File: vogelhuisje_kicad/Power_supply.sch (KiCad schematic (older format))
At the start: 8 parts, among them J1 Conn_01x02, J2 Conn_01x02_Female, J3 USB_C_Receptacle_USB2.0, P1 TP4056breakout, P2 GenericBoostConverter, Q1 Q_PMOS_GSD

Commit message: Update ESP_arduino.sch, Power_supply.sch, and 5 more files...
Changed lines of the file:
@@
 U 1 1 6263DE48
 P 2550 2300
-F 0 "P1" H 2575 2825 50  0000 C CNN
+F 0 "P?" H 2575 2825 50  0000 C CNN
 F 1 "TP4056breakout" H 2575 2734 50  0000 C CNN
 F 2 "Components:TP4056breakout" H 2500 2700 50  0001 C CNN
@@
 U 1 1 6263E192
 P 5450 2300
-F 0 "P2" H 5450 2715 50  0000 C CNN
+F 0 "P?" H 5450 2715 50  0000 C CNN
 F 1 "GenericBoostConverter" H 5450 2624 50  0000 C CNN
 F 2 "Components:GenericBoostConverter" H 5450 2450 50  0001 C CNN
@@
 U 1 1 6263EAD6
 P 3600 2250
-F 0 "R1" H 3670 2296 50  0000 L CNN
+F 0 "R?" H 3670 2296 50  0000 L CNN
 F 1 "100k" H 3670 2205 50  0000 L CNN
 F 2 "Resistor_THT:R_Axial_DIN0207_L6.3mm_D2.5mm_P7.62mm_Horizontal" V 3530 2250 50  0001 C CNN
@@
 U 1 1 6263EF5E
 P 1950 2400
-F 0 "#PWR0101" H 1950 2150 50  0001 C CNN
+F 0 "#PWR?" H 1950 2150 50  0001 C CNN
 F 1 "GND" H 1955 2227 50  0000 C CNN
 F 2 "" H 1950 2400 50  0001 C CNN
@@
 U 1 1 62643FC2
 P 3850 1900
-F 0 "D1" V 3896 1821 50  0000 R CNN
+F 0 "D?" V 3896 1821 50  0000 R CNN
 F 1 "D_Zener" V 3805 1821 50  0000 R CNN
 F 2 "Diode_SMD:D_SMB_Handsoldering" H 3850 1900 50  0001 C CNN
@@
 U 1 1 62647C4D
 P 3250 1200
-F 0 "J1" H 3168 875 50  0000 C CNN
+F 0 "J?" H 3168 875 50  0000 C CNN
 F 1 "Conn_01x02" H 3168 966 50  0000 C CNN
 F 2 "Connector_JST:JST_PH_B2B-PH-K_1x02_P2.00mm_Vertical" H 3250 1200 50  0001 C CNN
@@
 U 1 1 6264EDFF
 P 4100 1750
-F 0 "Q1" H 4305 1796 50  0000 L CNN
+F 0 "Q?" H 4305 1796 50  0000 L CNN
 F 1 "Q_PMOS_GSD" H 4305 1705 50  0000 L CNN
 F 2 "Package_TO_SOT_SMD:SOT-23" H 4300 1850 50  0001 C CNN
@@
 U 1 1 62654366
 P 5100 3300
-F 0 "J3" V 5253 4029 50  0000 L CNN
+F 0 "J?" V 5253 4029 50  0000 L CNN
 F 1 "USB_C_Receptacle_USB2.0" V 5162 4029 50  0000 L CNN
 F 2 "Connector_USB:USB_C_Receptacle_HRO_TYPE-C-31-M-12" H 5250 3300 50  0001 C CNN
@@
 U 1 1 62641E6A
 P 1650 2250
-F 0 "J2" H 1542 1925 50  0000 C CNN
+F 0 "J?" H 1542 1925 50  0000 C CNN
 F 1 "Conn_01x02_Female" H 1542 2016 50  0000 C CNN
 F 2 "Connector_PinSocket_2.54mm:PinSocket_1x02_P2.54mm_Vertical" H 1650 2250 50  0001 C CNN
@@
 U 1 1 62647069
 P 3600 2450
-F 0 "#PWR0102" H 3600 2200 50  0001 C CNN
+F 0 "#PWR?" H 3600 2200 50  0001 C CNN
 F 1 "GND" H 3605 2277 50  0000 C CNN
 F 2 "" H 3600 2450 50  0001 C CNN
@@
 U 1 1 626475C4
 P 6200 2450
-F 0 "#PWR0103" H 6200 2200 50  0001 C CNN
+F 0 "#PWR?" H 6200 2200 50  0001 C CNN
 F 1 "GND" H 6205 2277 50  0000 C CNN
 F 2 "" H 6200 2450 50  0001 C CNN

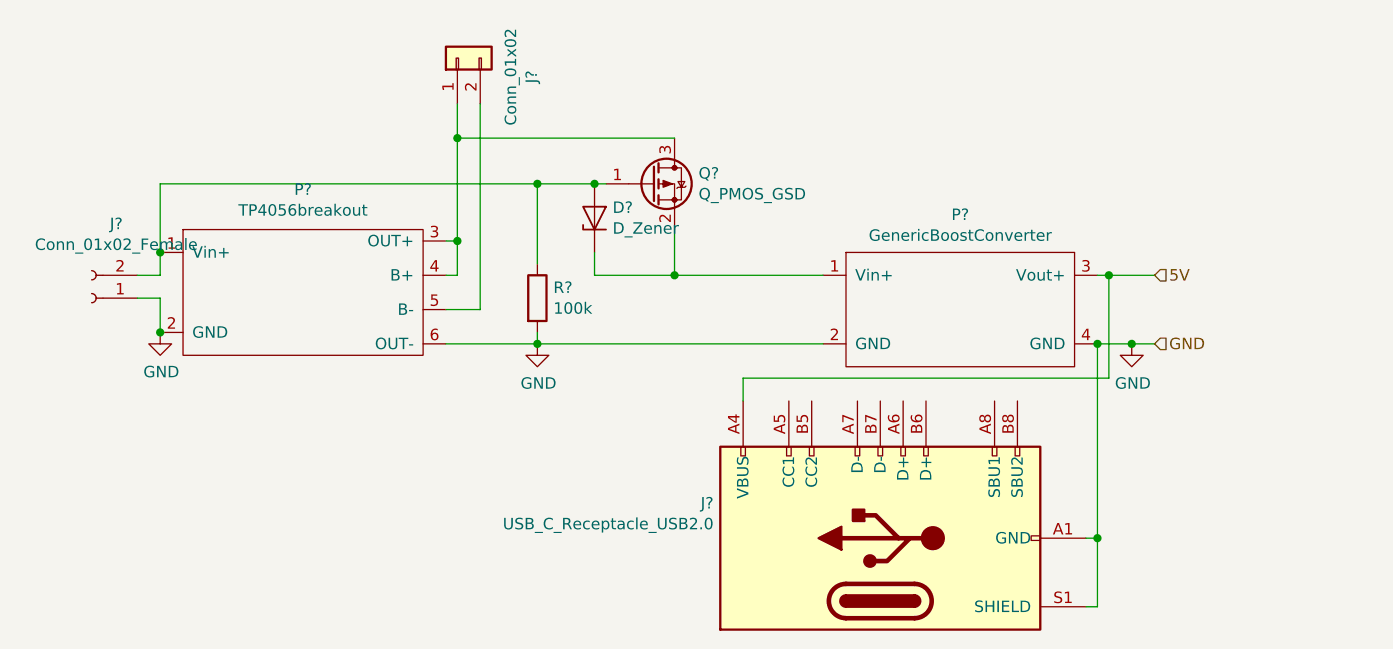
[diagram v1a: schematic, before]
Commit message: Add Camera to schematic
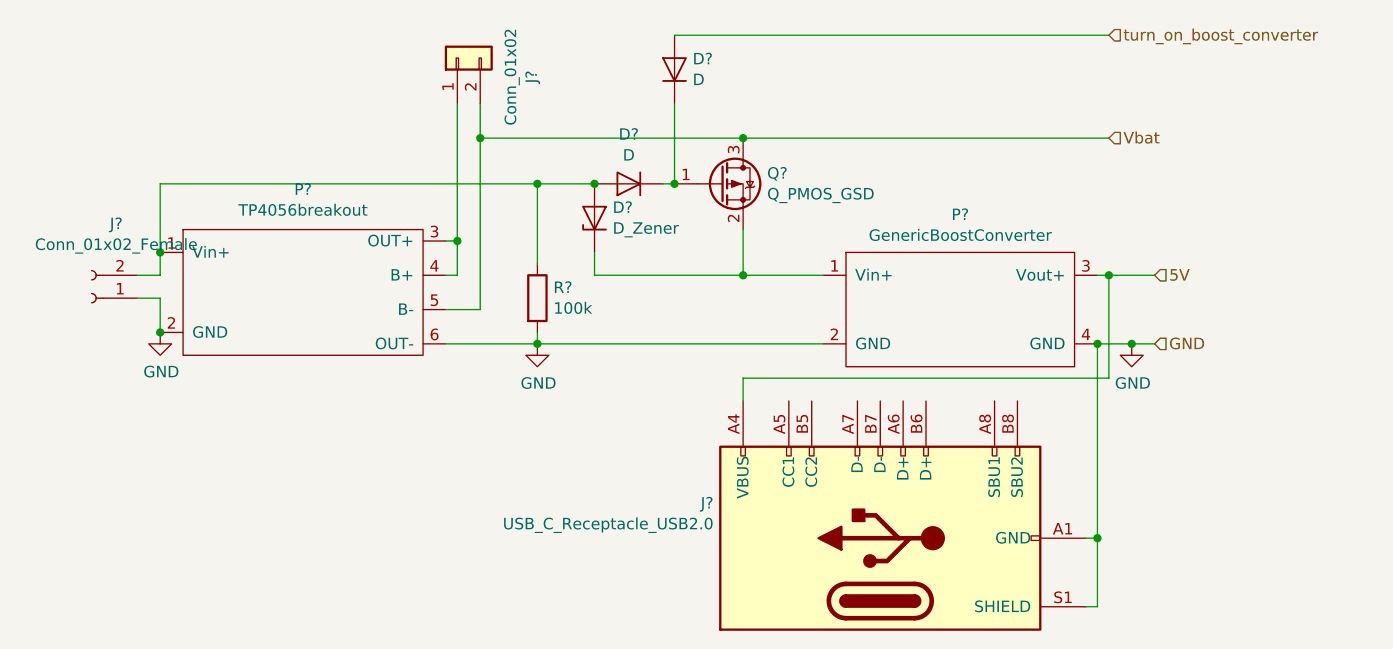
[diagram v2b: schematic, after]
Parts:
- added D? (x2): D, symbol Device:D
- renumbered D1 to D?, J2 to J?, J1 to J?, J3 to J?, P1 to P?, P2 to P?, Q1 to Q?, R1 to R?
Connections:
- net at D?.2 (A), J?.2 (Pin_2), P?.1 (Vin+)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: now also D?.2 (A); no longer Q?.1 (G)
- net at J?.1 (Pin_1), P?.3 (OUT+), P?.4 (B+): no longer Q?.3 (D)
- net Vbat: now reaches J?.2 (Pin_2), P?.5 (B-)
- net Vbat: now also Q?.3 (D)
- new net: D?.1 (K), D?.1 (K), Q?.1 (G)
- new net turn_on_boost_converter: D?.2 (A)
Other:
- moved on the sheet: Q?
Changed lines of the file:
@@
 $Descr A4 11693 8268
 encoding utf-8
-Sheet 2 3
+Sheet 2 4
 Title ""
 Date ""
@@
 $EndDescr
 $Comp
-L TP4056-breakout:TP4056breakout P1
+L TP4056-breakout:TP4056breakout P?
 U 1 1 6263DE48
 P 2550 2300
@@
 $EndComp
 $Comp
-L TP4056-breakout:GenericBoostConverter P2
+L TP4056-breakout:GenericBoostConverter P?
 U 1 1 6263E192
 P 5450 2300
@@
 $EndComp
 $Comp
-L Device:R R1
+L Device:R R?
 U 1 1 6263EAD6
 P 3600 2250
@@
 	1950 1750 1950 2050
 $Comp
-L power:GND #PWR0101
+L power:GND #PWR?
 U 1 1 6263EF5E
 P 1950 2400
@@
 $EndComp
 Wire Wire Line
-	3350 1400 3350 2300
-Wire Wire Line
 	3350 2300 3200 2300
 Wire Wire Line
@@
 Wire Wire Line
 	3600 1750 3850 1750
-Wire Wire Line
-	4200 1950 4200 2150
-Wire Wire Line
-	4200 2150 4850 2150
-$Comp
-L Device:D_Zener D1
-U 1 1 62643FC2
-P 3850 1900
-F 0 "D?" V 3896 1821 50  0000 R CNN
-F 1 "D_Zener" V 3805 1821 50  0000 R CNN
-F 2 "Diode_SMD:D_SMB_Handsoldering" H 3850 1900 50  0001 C CNN
-F 3 "~" H 3850 1900 50  0001 C CNN
-	1    3850 1900
-	0    -1   -1   0
-$EndComp
-Connection ~ 3850 1750
-Wire Wire Line
-	3850 1750 3900 1750
-Wire Wire Line
-	3850 2050 3850 2150
-Wire Wire Line
-	3850 2150 4200 2150
-Connection ~ 4200 2150
-$Comp
-L Connector_Generic:Conn_01x02 J1
+$Comp
+L Connector_Generic:Conn_01x02 J?
 U 1 1 62647C4D
 P 3250 1200
@@
 Connection ~ 3250 2000
 Wire Wire Line
-	3250 2000 3250 1550
-Wire Wire Line
 	3600 1750 1950 1750
 Connection ~ 3600 1750
 Wire Wire Line
 	3250 2000 3250 2150
-Wire Wire Line
-	4200 1550 3250 1550
-Connection ~ 3250 1550
-Wire Wire Line
-	3250 1550 3250 1400
-$Comp
-L Device:Q_PMOS_GSD Q1
-U 1 1 6264EDFF
-P 4100 1750
-F 0 "Q?" H 4305 1796 50  0000 L CNN
-F 1 "Q_PMOS_GSD" H 4305 1705 50  0000 L CNN
-F 2 "Package_TO_SOT_SMD:SOT-23" H 4300 1850 50  0001 C CNN
-F 3 "~" H 4100 1750 50  0001 C CNN
-	1    4100 1750
-	1    0    0    -1
-$EndComp
-$Comp
-L Connector:USB_C_Receptacle_USB2.0 J3
+$Comp
+L Connector:USB_C_Receptacle_USB2.0 J?
 U 1 1 62654366
 P 5100 3300
@@
 	6050 2450 6200 2450
 $Comp
-L Connector:Conn_01x02_Female J2
+L Connector:Conn_01x02_Female J?
 U 1 1 62641E6A
 P 1650 2250
@@
 Connection ~ 1950 2050
 $Comp
-L power:GND #PWR0102
+L power:GND #PWR?
 U 1 1 62647069
 P 3600 2450
@@
 $EndComp
 $Comp
-L power:GND #PWR0103
+L power:GND #PWR?
 U 1 1 626475C4
 P 6200 2450
@@
 Text HLabel 6300 2450 2    50   Input ~ 0
 GND
+Wire Wire Line
+	3850 2050 3850 2150
+$Comp
+L Device:Q_PMOS_GSD Q?
+U 1 1 6264EDFF
+P 4400 1750
+F 0 "Q?" H 4605 1796 50  0000 L CNN
+F 1 "Q_PMOS_GSD" H 4605 1705 50  0000 L CNN
+F 2 "Package_TO_SOT_SMD:SOT-23" H 4600 1850 50  0001 C CNN
+F 3 "~" H 4400 1750 50  0001 C CNN
+	1    4400 1750
+	1    0    0    -1
+$EndComp
+$Comp
+L Device:D_Zener D?
+U 1 1 62643FC2
+P 3850 1900
+F 0 "D?" V 3896 1821 50  0000 R CNN
+F 1 "D_Zener" V 3805 1821 50  0000 R CNN
+F 2 "Diode_SMD:D_SMB_Handsoldering" H 3850 1900 50  0001 C CNN
+F 3 "~" H 3850 1900 50  0001 C CNN
+	1    3850 1900
+	0    -1   -1   0
+$EndComp
+Wire Wire Line
+	4500 1950 4500 2150
+Connection ~ 4500 2150
+Wire Wire Line
+	4500 2150 4850 2150
+Wire Wire Line
+	3850 2150 4500 2150
+Wire Wire Line
+	3250 1400 3250 2000
+$Comp
+L Device:D D?
+U 1 1 626DAFFC
+P 4000 1750
+F 0 "D?" H 4000 1534 50  0000 C CNN
+F 1 "D" H 4000 1625 50  0000 C CNN
+F 2 "" H 4000 1750 50  0001 C CNN
+F 3 "~" H 4000 1750 50  0001 C CNN
+	1    4000 1750
+	-1   0    0    1
+$EndComp
+$Comp
+L Device:D D?
+U 1 1 626DB777
+P 4200 1250
+F 0 "D?" V 4246 1171 50  0000 R CNN
+F 1 "D" V 4155 1171 50  0000 R CNN
+F 2 "" H 4200 1250 50  0001 C CNN
+F 3 "~" H 4200 1250 50  0001 C CNN
+	1    4200 1250
+	0    -1   -1   0
+$EndComp
+Wire Wire Line
+	4500 1550 3350 1550
+Wire Wire Line
+	3350 1400 3350 1550
+Connection ~ 3350 1550
+Wire Wire Line
+	3350 1550 3350 2300
+Connection ~ 3850 1750
+Wire Wire Line
+	4150 1750 4200 1750
+Wire Wire Line
+	4200 1400 4200 1750
+Connection ~ 4200 1750
+Text HLabel 6100 1100 2    50   Input ~ 0
+turn_on_boost_converter
+Text HLabel 6100 1550 2    50   Input ~ 0
+Vbat
+Wire Wire Line
+	4500 1550 6100 1550
+Connection ~ 4500 1550
+Wire Wire Line
+	4200 1100 6100 1100
 $EndSCHEMATC
